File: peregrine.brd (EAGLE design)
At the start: 55.9 x 55.9 mm, 77 parts, among them IC2 LMV358IDGKR, J1 USB MICRO, Q1 BSS123, Q10 BSS123, Q11 BSS123, Q2 BSS123, U1 ITG-3200, U2 ADXL345, U5 ATMEGA32U4-XUAU, Y1 16MHz KX-7

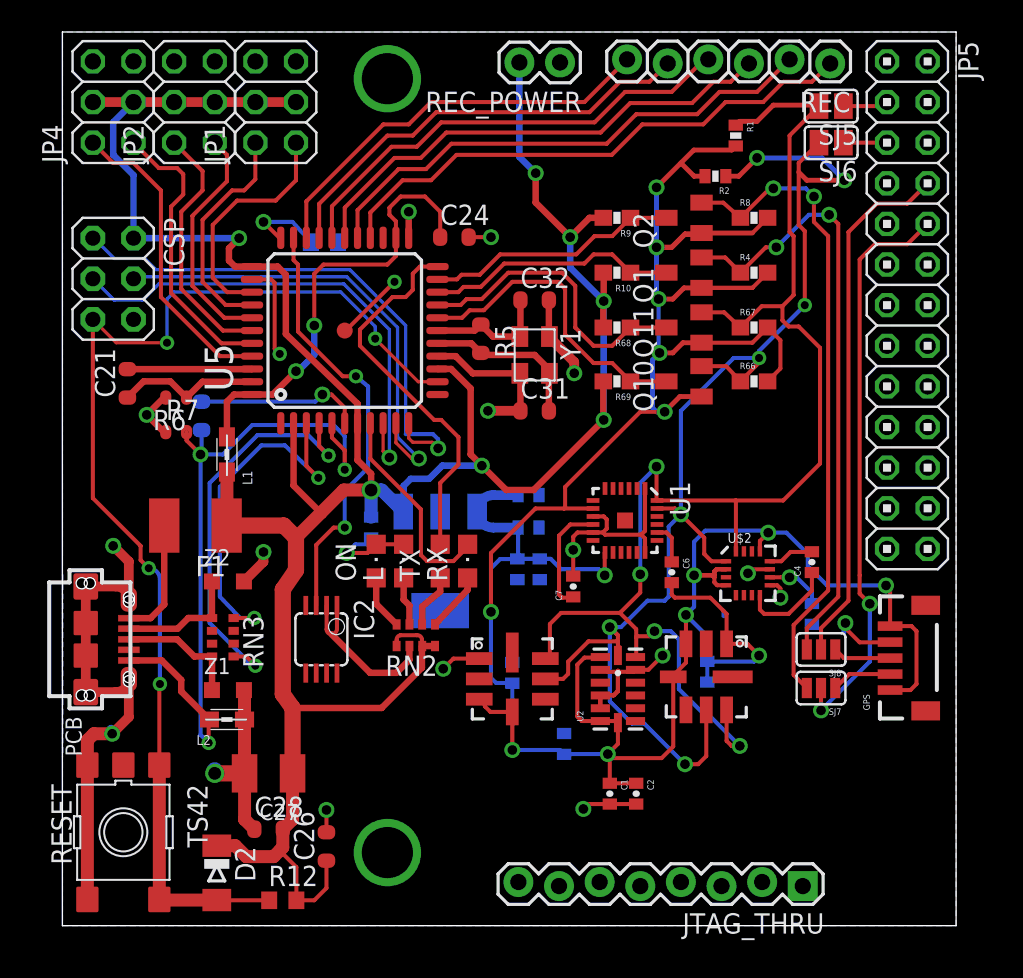
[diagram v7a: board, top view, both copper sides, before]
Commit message: Fixed silk
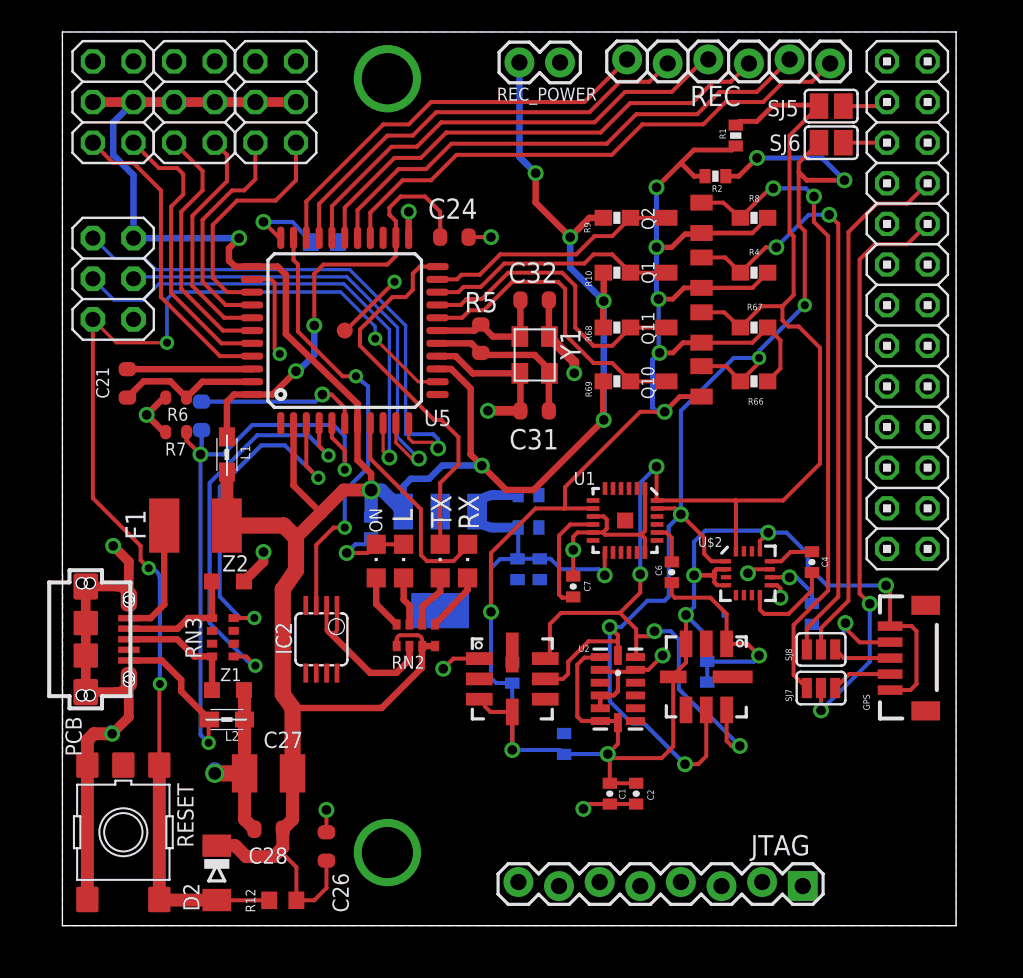
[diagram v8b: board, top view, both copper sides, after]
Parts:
- renumbered JTAG_THRU to JTAG
